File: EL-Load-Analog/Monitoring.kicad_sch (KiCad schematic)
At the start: 73 parts, among them K2 EE2-5TNU, Q1 2N7002, Q2 2N7002, Q301 2N7002, U1 SN74LVC1G3157DBV, U301 LM833, U302 LM833, U303 OPA189/MCP6V51/LTC2050HV, U304 OPA189/MCP6V51/LTC2050HV, U305 74HCT02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

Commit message: Working on #4,#2 fixed #8,#22
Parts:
- C316: Part Name C_2.2uF_10V_X7R_10%_0805 -> C_2.2uF_25V_X7R_10%_0805
- R18, R19: value 100k -> 470; Part Name R_100.0kΩ_0805_1% -> R_470.0Ω_0805_1%
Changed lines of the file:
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@@
       (effects (font (size 1.27 1.27)) hide)
     )
-    (property "Part Name" "C_2.2uF_10V_X7R_10%_0805" (at 76.2 124.46 0)
+    (property "Part Name" "C_2.2uF_25V_X7R_10%_0805" (at 76.2 124.46 0)
       (effects (font (size 1.27 1.27)) hide)
     )
@@
       (effects (font (size 1.27 1.27)))
     )
-    (property "Value" "100k" (at 180.34 81.28 90)
+    (property "Value" "470" (at 180.34 81.28 90)
       (effects (font (size 1.27 1.27)))
     )
@@
       (effects (font (size 1.27 1.27)) hide)
     )
-    (property "Part Name" "R_100.0kΩ_0805_1%" (at 180.34 78.74 0)
+    (property "Part Name" "R_470.0Ω_0805_1%" (at 180.34 78.74 0)
       (effects (font (size 1.27 1.27)) hide)
     )
@@
       (effects (font (size 1.27 1.27)))
     )
-    (property "Value" "100k" (at 198.755 15.875 90)
+    (property "Value" "470" (at 198.755 15.875 90)
       (effects (font (size 1.27 1.27)))
     )
@@
       (effects (font (size 1.27 1.27)) hide)
     )
-    (property "Part Name" "R_100.0kΩ_0805_1%" (at 198.755 18.415 0)
-      (effects (font (size 1.27 1.27)) hide)
-    )
+    (property "Part Name" "R_470.0Ω_0805_1%" (at 198.755 18.415 0)
+      (effects (font (size 1.27 1.27)) hide)
+    )

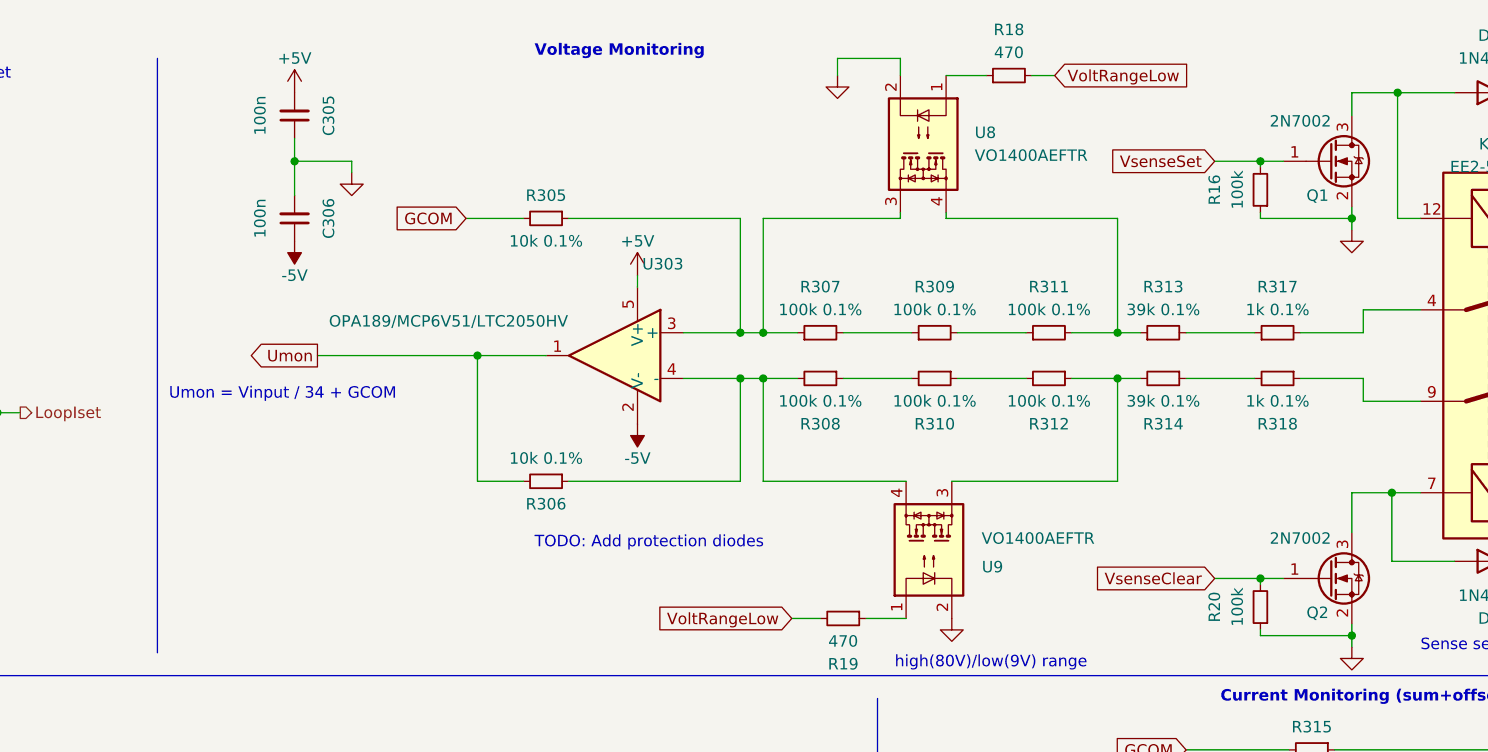
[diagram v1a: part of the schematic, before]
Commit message: Fixing issues from #4, adding ESD protection (#6)
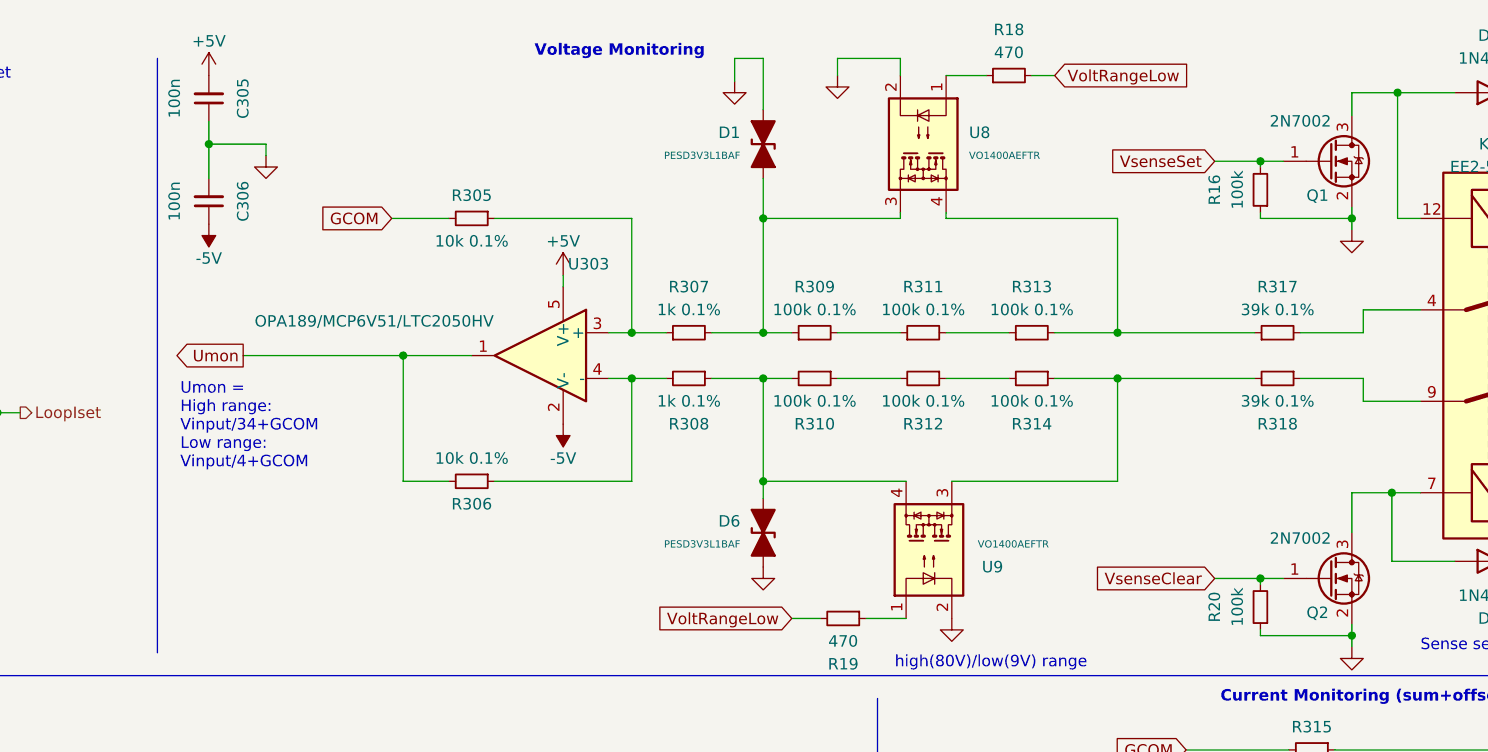
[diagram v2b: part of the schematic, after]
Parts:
- added D1, D6: PESD3V3L1BAF, Diode_SMD:D_SOD-323, symbol Device:D_TVS_Filled
- R307, R308: value 100k 0.1% -> 1k 0.1%; Part Name R_100k_0805_0.1% -> R_1k_0805_0.1%
- R313, R314: value 39k 0.1% -> 100k 0.1%; Part Name R_39k_0805_0.1% -> R_100k_0805_0.1%
- R317, R318: value 1k 0.1% -> 39k 0.1%; Part Name R_1k_0805_0.1% -> R_39k_0805_0.1%
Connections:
- net GND: now also D1.2 (A2), D6.1 (A1)
- net at R314.1, R318.2: now also U9.3
- net at R312.1, R314.2: no longer U9.3
- net at R308.1, R310.2: now also U9.4, D6.2 (A2)
- net at R306.1, R308.2, U303.4 (-): no longer U9.4
- net at R305.1, R307.1, U303.3 (+): no longer U8.3
- net at R313.2, R317.1: now also U8.4
- net at R307.2, R309.1: now also U8.3, D1.1 (A1)
- net at R311.2, R313.1: no longer U8.4
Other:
- note added: "Umon = High range: Vinput/34+GCOM Low range: Vinput/4+GCOM"
- note removed: "TODO: Add protection diodes"
- note removed: "Umon = Vinput / 34 + GCOM"
- moved on the sheet: C305, C306, R305, R306, R307, R308, R309, R310, R311, R312, R313, R314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

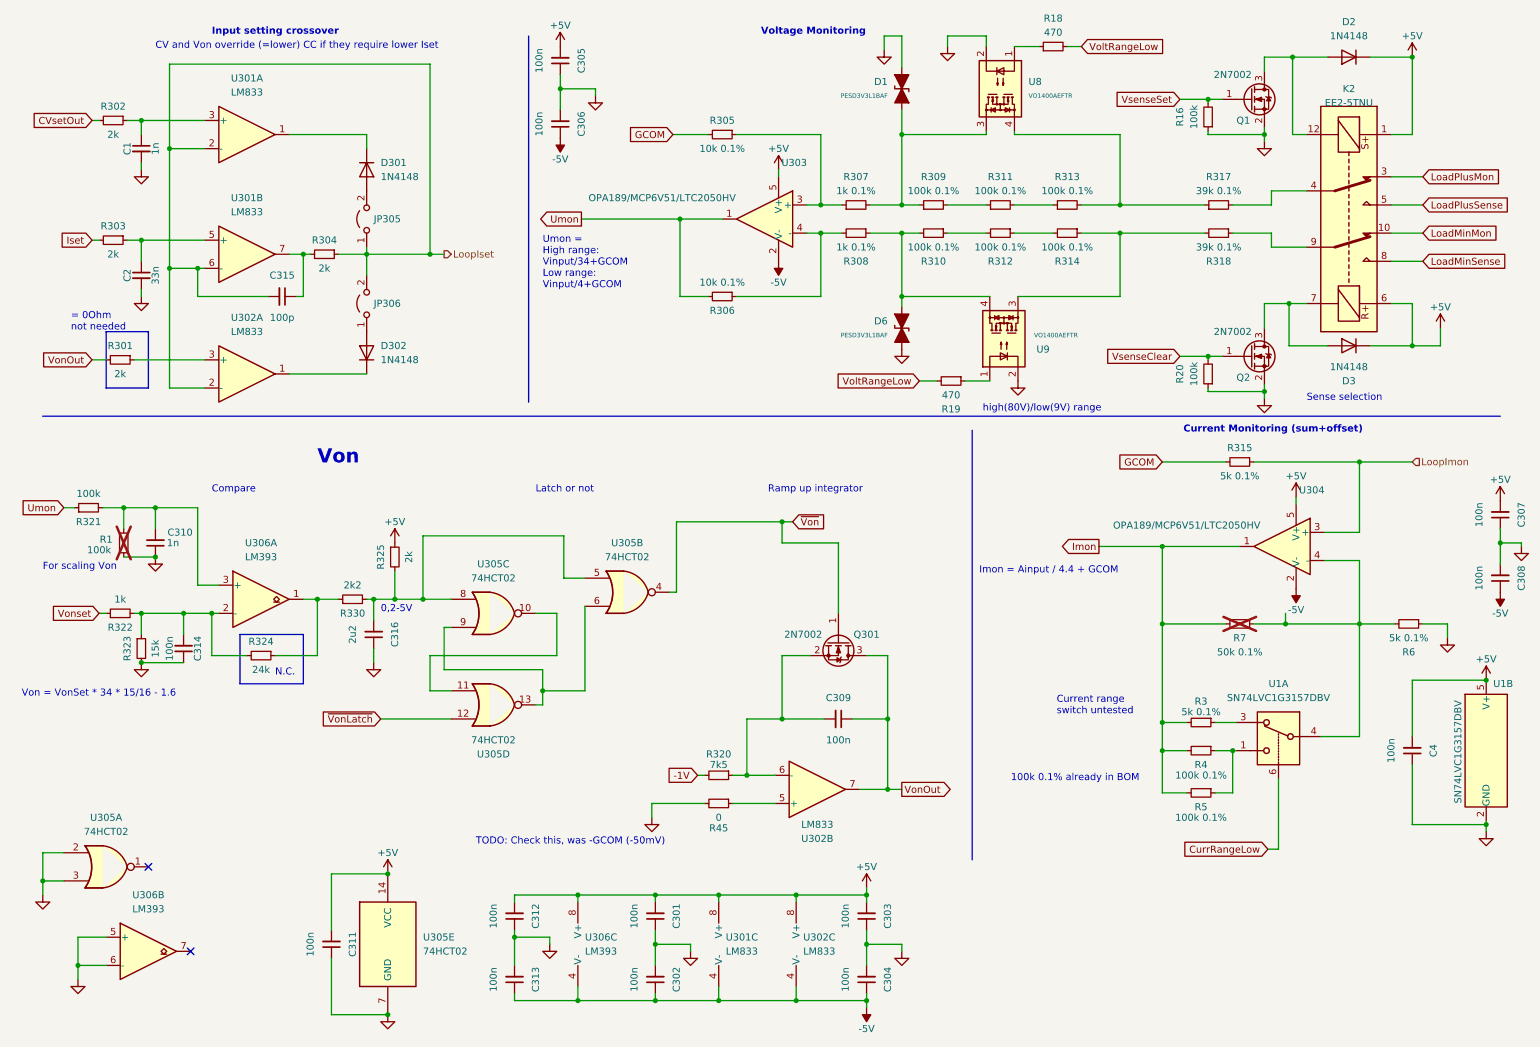
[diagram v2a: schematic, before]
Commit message: Added heatsink moutingholes, reverse polarity, moved snubbers.
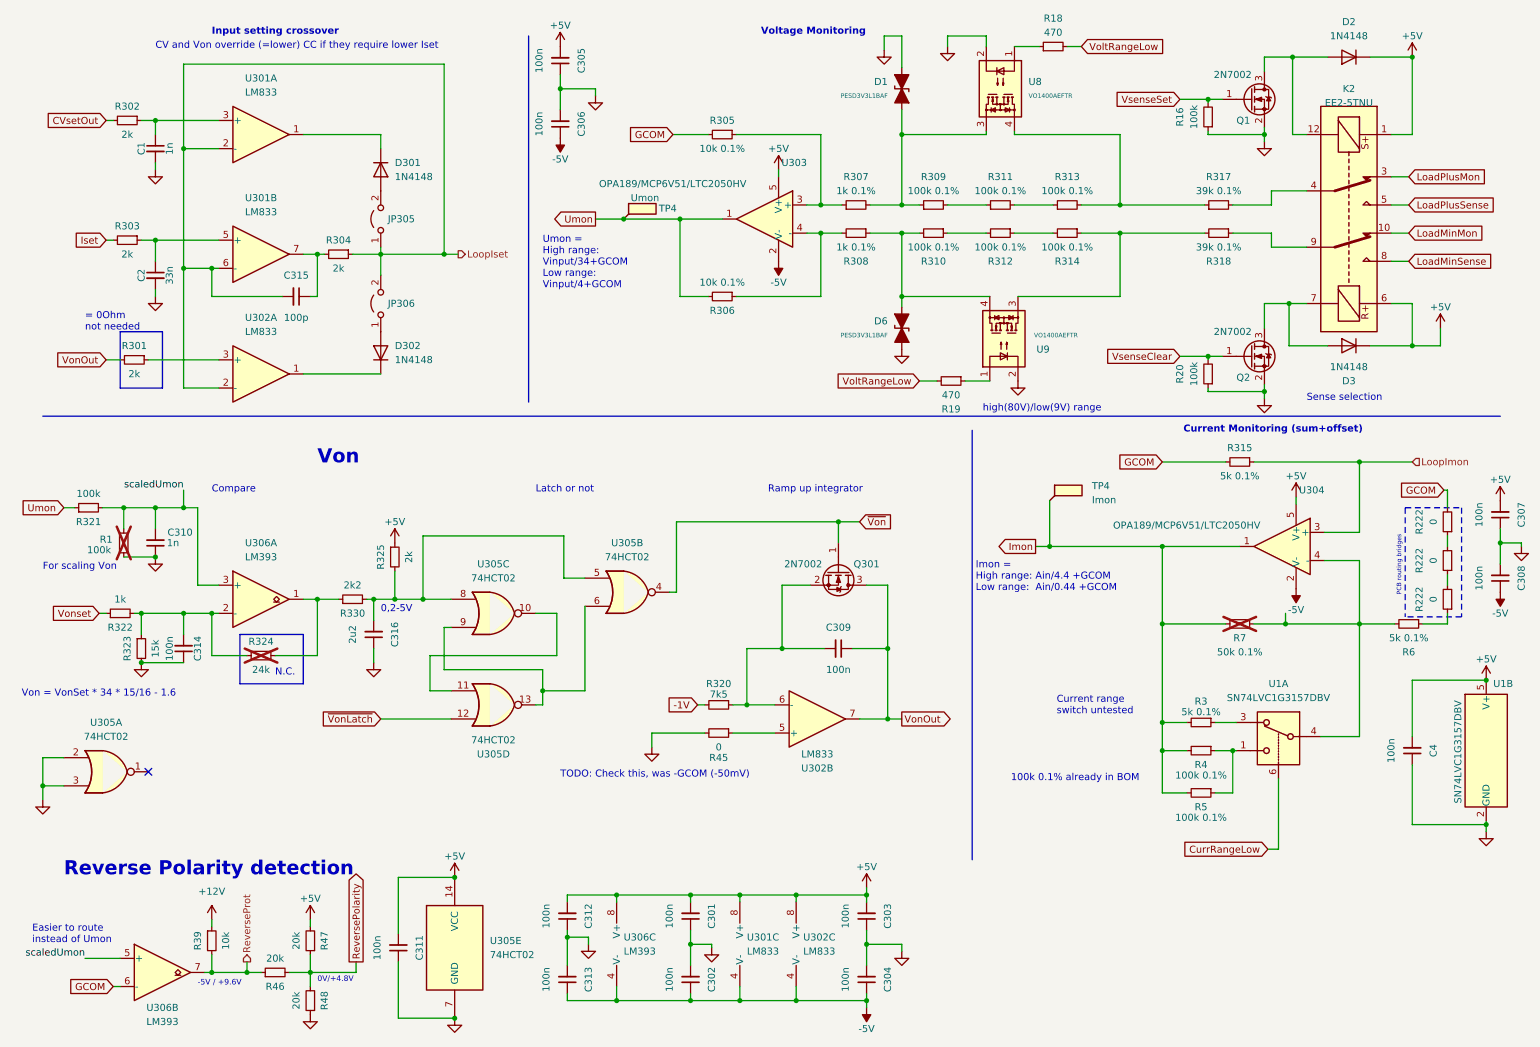
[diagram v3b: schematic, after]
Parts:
- added R222 (x3): 0, Resistor_SMD:R_0805_2012Metric, symbol Device:R_Small
- added R39: 10k, Resistor_SMD:R_0805_2012Metric, symbol Device:R_Small
- added R46, R47, R48: 20k, Resistor_SMD:R_0805_2012Metric, symbol Device:R_Small
- added TP4: Imon, TestPoint:TestPoint_Pad_1.0x1.0mm, symbol Connector:TestPoint_Flag
- added TP4: Umon, TestPoint:TestPoint_Pad_1.0x1.0mm, symbol Connector:TestPoint_Flag
- R324: now not fitted; now left out of the parts list
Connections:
- net +5V: now also R47.2
- net GCOM: now also U306.6 (-), R222.2
- net GND: now also R48.1; no longer R6.1, U306.5 (+), U306.6 (-)
- net Imon: now also TP4.1
- net Umon: now also TP4.1
- net scaledUmon: now reaches C310.2, R1.2, R321.2, U306.3 (+)
- net scaledUmon: now also U306.5 (+)
- net ReverseProt: now reaches U306.7
- net ReverseProt: now also R39.2, R46.1
- new net: R222.1, R6.1
- new net: R222.1, R222.2 (x2)
- new net +12V: R39.1
- new net ReversePolarity: R46.2, R47.1, R48.2
- no-connect marks 2 -> 1
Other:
- note added: "-5V / +9.6V"
- note added: "0V/+4.8V"
- note added: "Easier to route instead of Umon"
- note added: "Imon = High range: Ain/4.4 +GCOM Low range: Ain/0.44 +GCOM"
- note added: "PCB routing bridges"
- note added: "Reverse Polarity detection"
- note removed: "Imon = Ainput / 4.4 + GCOM"
- moved on the sheet: C1, C2, C301, C302, C309, C311, C312, C313, C315, D301, D302, JP305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

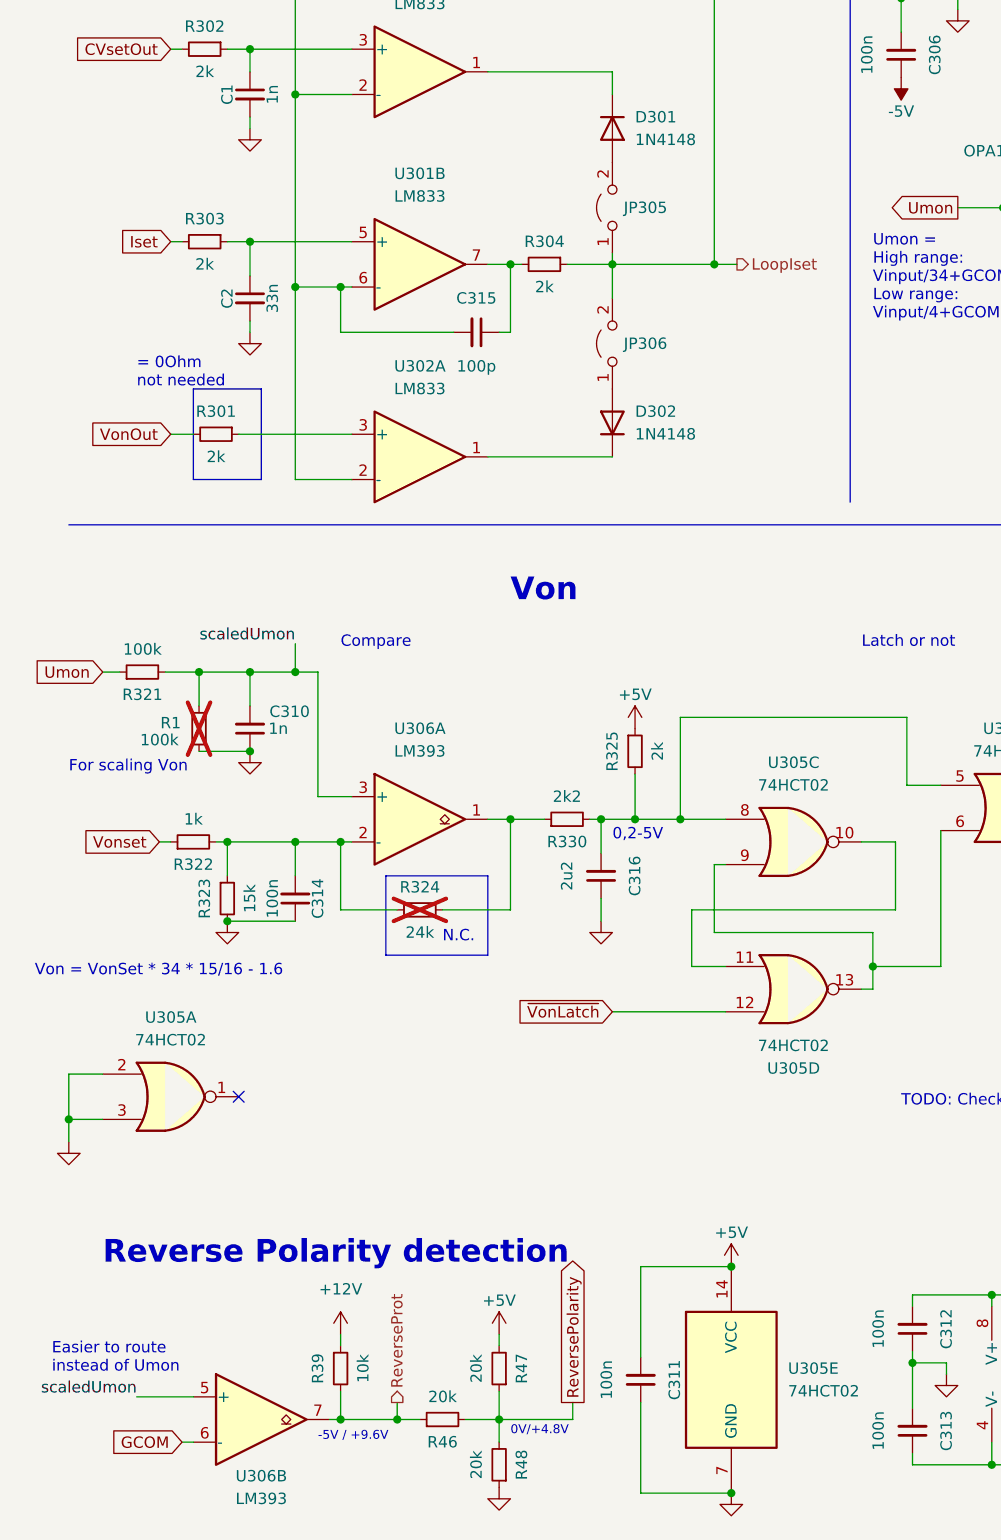
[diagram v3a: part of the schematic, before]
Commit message: v4 Analog board design. Features reverse polarity, remote sense error and new clamping circuitry.
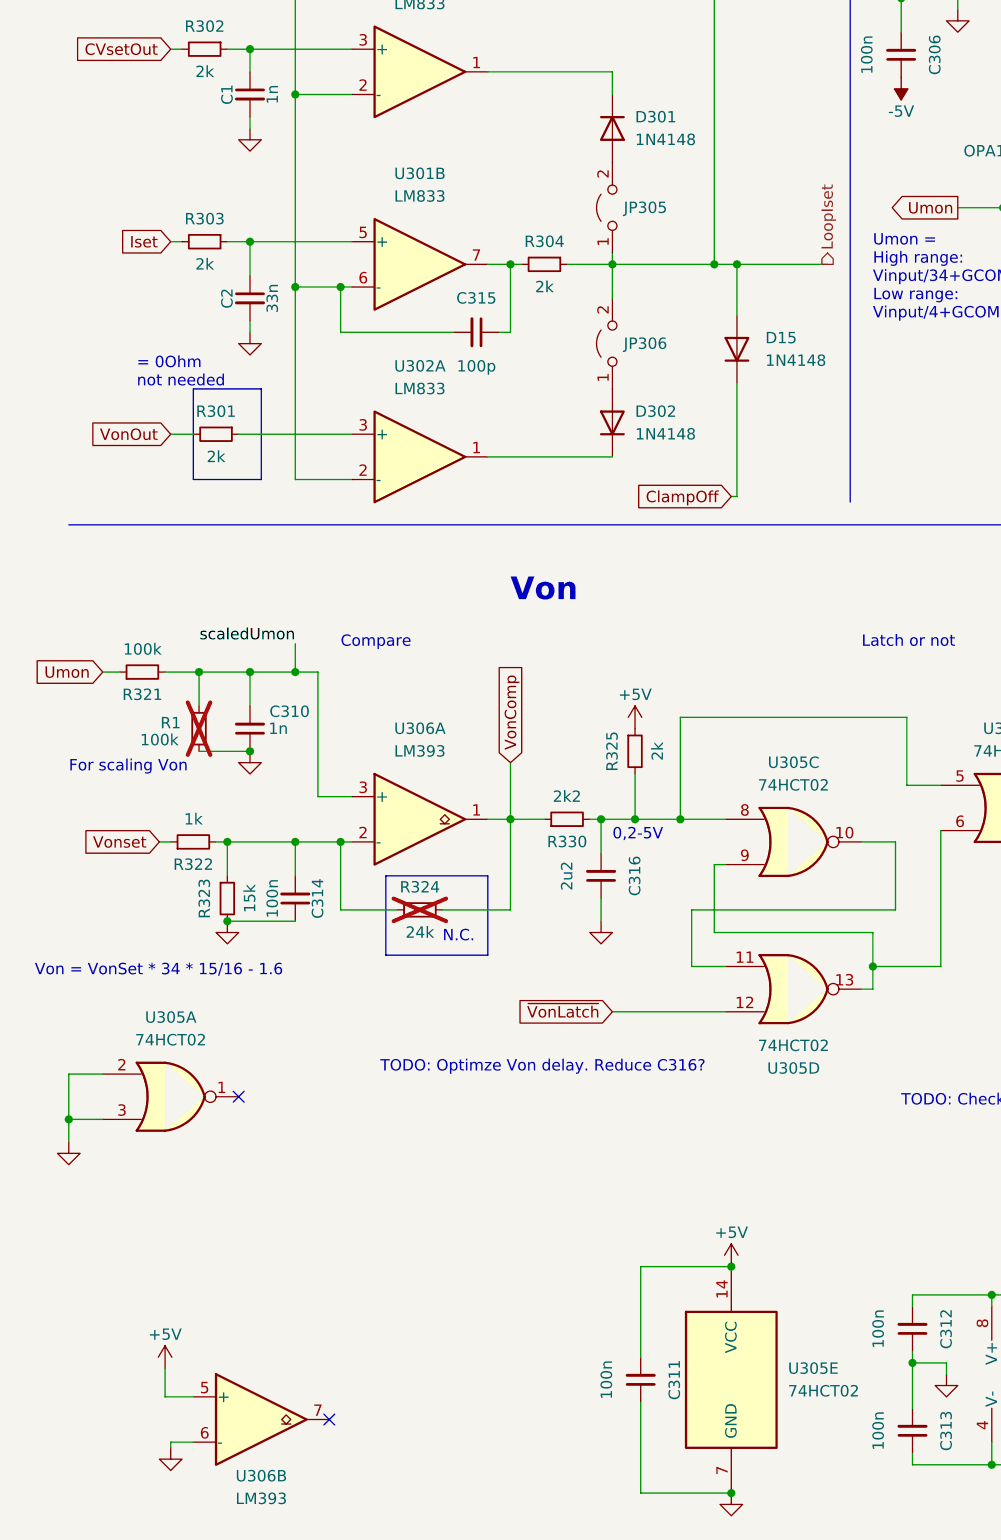
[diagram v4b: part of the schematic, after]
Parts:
- removed R39: 10k, Resistor_SMD:R_0805_2012Metric, symbol Device:R_Small
- removed R46, R47, R48: 20k, Resistor_SMD:R_0805_2012Metric, symbol Device:R_Small
- added D15: 1N4148, Diode_SMD:D_MiniMELF, symbol Diode:1N4148
- C301, C302, C303, C304, C305, C306, C307, C308, C309, C311, C312, C313, C314, C4: Part Name C_100.0nF_0805_20% -> C_100.0nF_50V_0805_10%_X7R
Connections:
- net +5V: now also U306.5 (+)
- net GCOM: no longer U306.6 (-)
- net GND: now also U306.6 (-)
- net LoopIset: now also D15.2 (A)
- net scaledUmon: no longer U306.5 (+)
- net VonComp: now reaches R324.1, R330.1, U306.1
- net ReverseProt: no longer names the net of U306.7
- new net ClampOff: D15.1 (K)
- no-connect marks 1 -> 2
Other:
- note added: "TODO: Optimze Von delay. Reduce C316?"
- note removed: "-5V / +9.6V"
- note removed: "0V/+4.8V"
- note removed: "Easier to route instead of Umon"
- note removed: "Reverse Polarity detection"
